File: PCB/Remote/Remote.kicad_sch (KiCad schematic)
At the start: 46 parts, among them J1 LCD, J2 DC, J3 TEMP, J4 LCD, J5 Reset, J6 USB-C-Socket-H, J7 TC2030-USB-NL-DS, U1 ESP32-S3-MINI-1, U2 SCD41, U3 MD8942, U4 TMP1075DSG, U5 GZP6816D, U8 VEML6040

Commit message: Moved PCB here
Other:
- title: 2" LCD -> Remote
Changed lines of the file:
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@@
 	(paper "A4")
 	(title_block
-		(title "2\" LCD")
+		(title "Remote")
 		(company "Adrian Kennard / Andrews & Arnold Ltd")
 		(comment 1 "@TheRealRevK")

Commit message: Case
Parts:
- D4: footprint RevK:SMD1010 -> RevK:SMD1010-Side
- U4: footprint Package_SON:WSON-8-1EP_2x2mm_P0.5mm_EP0.9x1.6mm_ThermalVias -> RevK:WSON-8-1EP_2x2mm_P0.5mm_EP0.9x1.6mm_ThermalVias-Side
- U8: footprint RevK:VEML6040 -> RevK:VEML6040-Side
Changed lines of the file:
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@@
 			)
 		)
-		(property "Footprint" "Package_SON:WSON-8-1EP_2x2mm_P0.5mm_EP0.9x1.6mm_ThermalVias"
+		(property "Footprint" "RevK:WSON-8-1EP_2x2mm_P0.5mm_EP0.9x1.6mm_ThermalVias-Side"
 			(at 252.73 116.84 0)
 			(effects
@@
 			)
 		)
-		(property "Footprint" "RevK:SMD1010"
+		(property "Footprint" "RevK:SMD1010-Side"
 			(at 162.56 43.815 0)
 			(effects
@@
 			)
 		)
-		(property "Footprint" "RevK:VEML6040"
+		(property "Footprint" "RevK:VEML6040-Side"
 			(at 254 126.365 0)
 			(effects

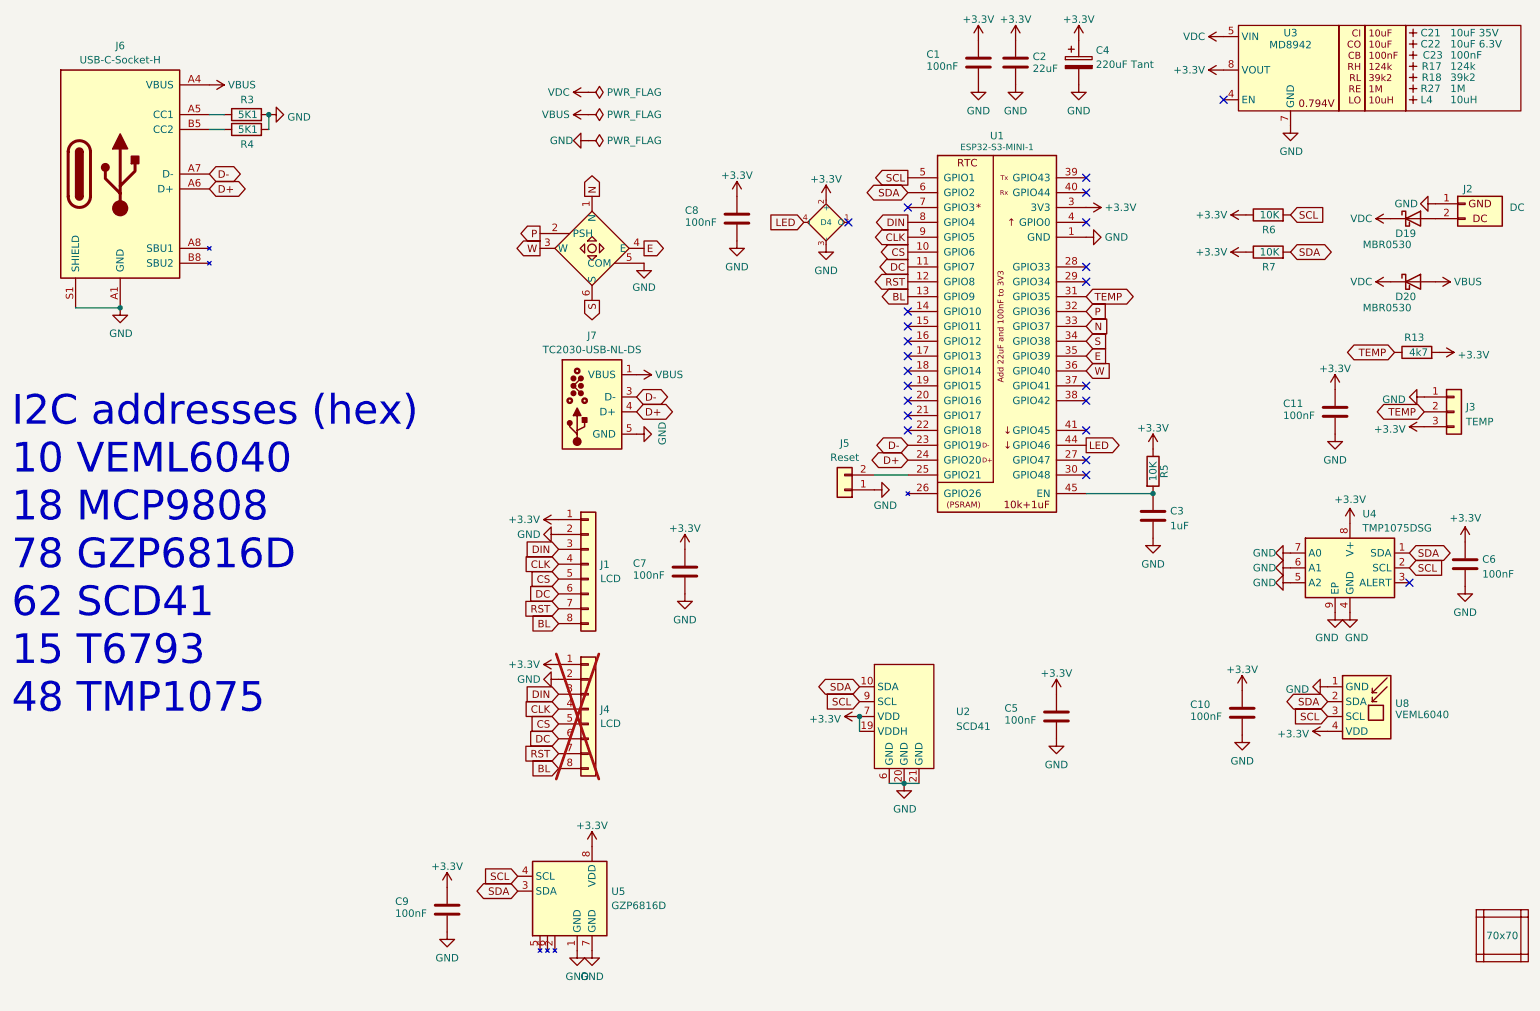
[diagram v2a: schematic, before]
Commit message: Change to SHT so humidity when no CO2
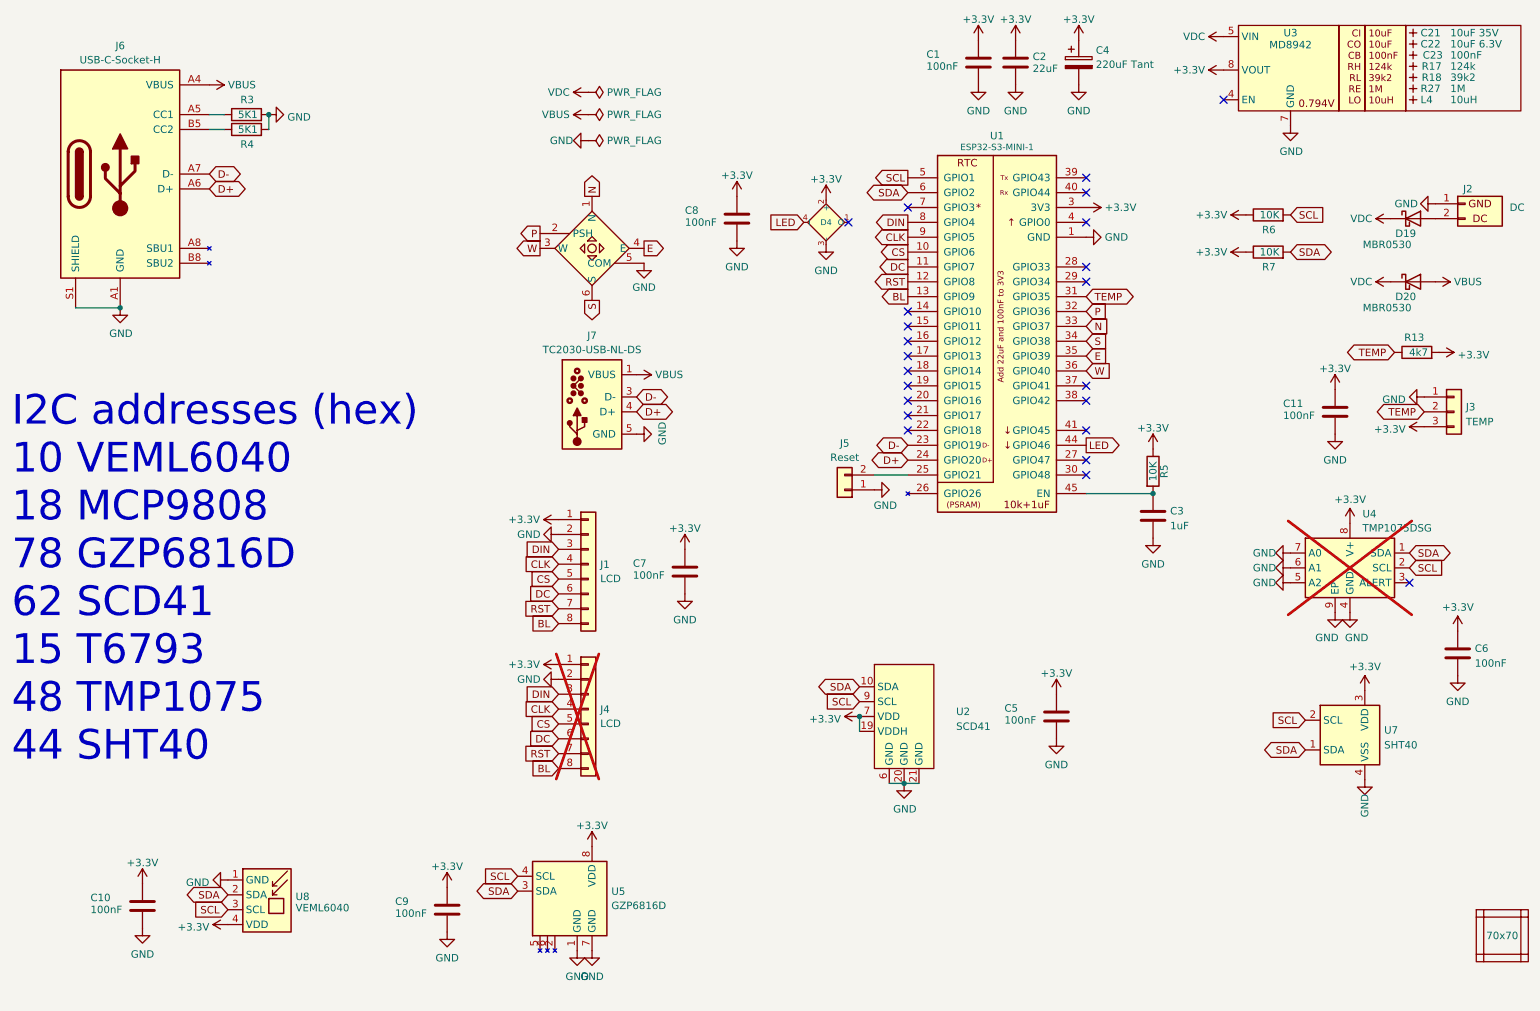
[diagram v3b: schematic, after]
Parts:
- added U7: SHT40, RevK:Sensirion_DFN-4_1.5x1.5mm_P0.5mm_SHT4x, symbol RevK:SHT40
- U4: now not fitted; now left out of the parts list
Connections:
- net +3.3V: now also U7.3 (VDD)
- net GND: now also U7.4 (VSS)
- net SCL: now also U7.2 (SCL)
- net SDA: now also U7.1 (SDA)
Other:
- note added: "I2C addresses (hex) 10 VEML6040 18 MCP9808 78 GZP6816D 62 SCD41 15 T6793 48 TMP1075 44 SHT40"
- note removed: "I2C addresses (hex) 10 VEML6040 18 MCP9808 78 GZP6816D 62 SCD41 15 T6793 48 TMP1075"
- moved on the sheet: C10, C6, U8

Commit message: Latest render
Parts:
- R13: MPN (none) -> C25900
- R17: MPN (none) -> C2933070
- R18: MPN (none) -> C7467415
- R27: MPN (none) -> C26083
- R3, R4: MPN (none) -> C25905
- R5, R6, R7: MPN (none) -> C25744
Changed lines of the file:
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@@
 			)
 		)
+		(property "MPN" "C25905"
+			(at 62.23 35.56 90)
+			(effects
+				(font
+					(size 1.27 1.27)
+				)
+				(hide yes)
+			)
+		)
 		(pin "1"
 		)
@@
 			)
 		)
+		(property "MPN" "C25905"
+			(at 62.23 33.02 90)
+			(effects
+				(font
+					(size 1.27 1.27)
+				)
+				(hide yes)
+			)
+		)
 		(pin "1"
 		)
@@
 			)
 		)
+		(property "MPN" "C25900"
+			(at 262.255 73.66 90)
+			(effects
+				(font
+					(size 1.27 1.27)
+				)
+				(hide yes)
+			)
+		)
 		(pin "1"
 		)
@@
 			)
 		)
+		(property "MPN" "C25744"
+			(at 236.855 50.165 90)
+			(effects
+				(font
+					(size 1.27 1.27)
+				)
+				(hide yes)
+			)
+		)
 		(pin "1"
 		)
@@
 			)
 		)
-		(property "Part No" ""
-			(at 261.62 28.575 0)
-			(effects
-				(font
-					(size 1.27 1.27)
-				)
-				(hide yes)
-			)
-		)
-		(property "Note" ""
+		(property "MPN" "C26083"
 			(at 261.62 28.575 0)
 			(effects
@@
 			)
 		)
-		(property "Part No" ""
-			(at 261.62 24.765 0)
-			(effects
-				(font
-					(size 1.27 1.27)
-				)
-				(hide yes)
-			)
-		)
-		(property "Note" ""
+		(property "MPN" "C2933070"
 			(at 261.62 24.765 0)
 			(effects
@@
 			)
 		)
+		(property "MPN" "C25744"
+			(at 217.17 93.98 90)
+			(effects
+				(font
+					(size 1.27 1.27)
+				)
+				(hide yes)
+			)
+		)
 		(pin "1"
 		)
@@
 			)
 		)
-		(property "Part No" ""
-			(at 261.62 26.67 0)
-			(effects
-				(font
-					(size 1.27 1.27)
-				)
-				(hide yes)
-			)
-		)
-		(property "Note" ""
-			(at 261.62 26.67 0)
+		(property "MPN" "C7467415"
+			(at 261.62 26.67 90)
 			(effects
 				(font
@@
 			(effects
 				(font
+					(size 1.27 1.27)
+				)
+				(hide yes)
+			)
+		)
+		(property "MPN" "C25744"
+			(at 236.855 56.515 90)
+			(effects
+				(font

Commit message: Tweaks
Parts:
- U5: footprint Package_LGA:Bosch_LGA-8_2x2.5mm_P0.65mm_ClockwisePinNumbering -> RevK:Bosch_LGA-8_2x2.5mm_P0.65mm_ClockwisePinNumbering
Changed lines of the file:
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@@
 			)
 		)
-		(property "Footprint" "Package_LGA:Bosch_LGA-8_2x2.5mm_P0.65mm_ClockwisePinNumbering"
+		(property "Footprint" "RevK:Bosch_LGA-8_2x2.5mm_P0.65mm_ClockwisePinNumbering"
 			(at 118.745 186.055 0)
 			(effects

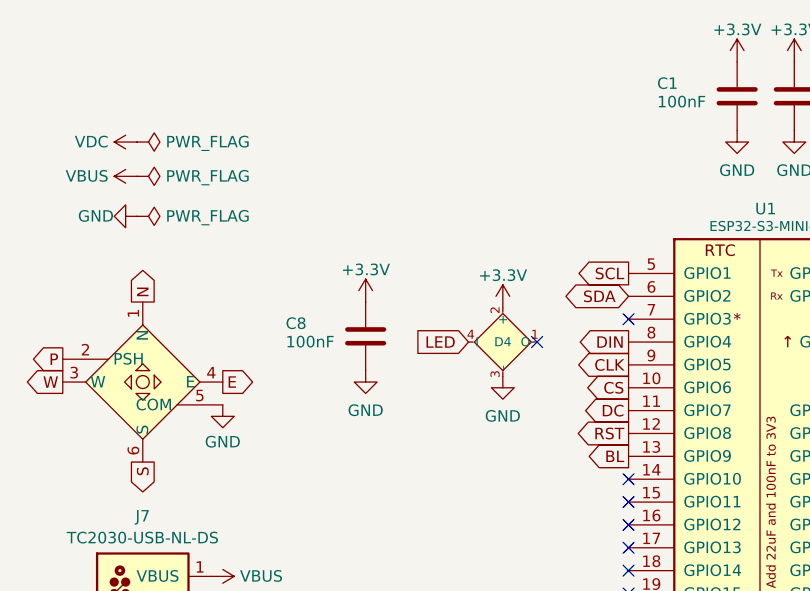
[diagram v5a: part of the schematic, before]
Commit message: More LEDs
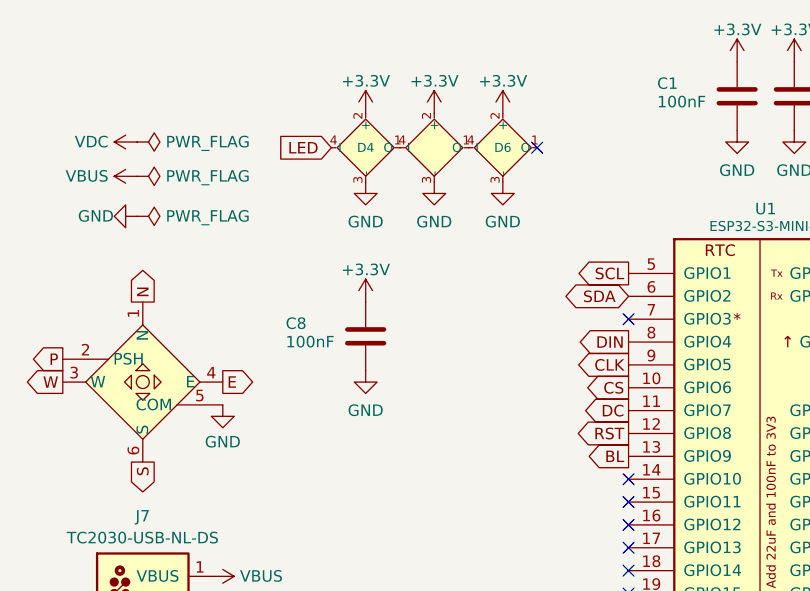
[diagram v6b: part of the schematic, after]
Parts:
- added D5, D6: XL-1010RGBC-WS2812B, RevK:SMD1010-Side, symbol RevK:WS2812B-1mm
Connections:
- net +3.3V: now also D5.2 (+), D6.2 (+)
- net GND: now also D5.3 (-), D6.3 (-)
- net at D4.1 (O): now also D5.4 (I)
- new net: D5.1 (O), D6.4 (I)
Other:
- moved on the sheet: D4

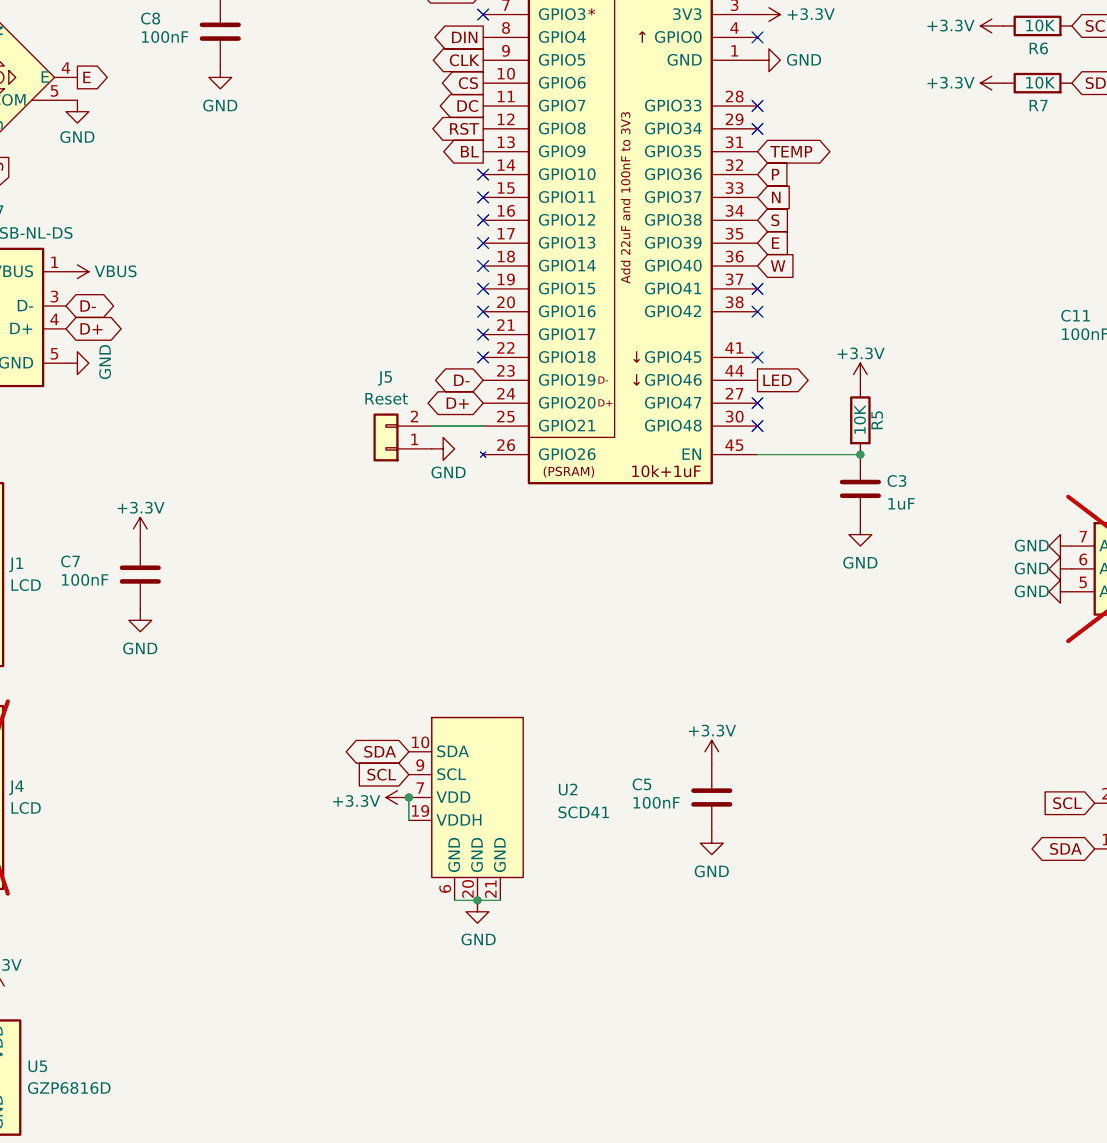
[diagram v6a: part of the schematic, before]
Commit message: Mic added
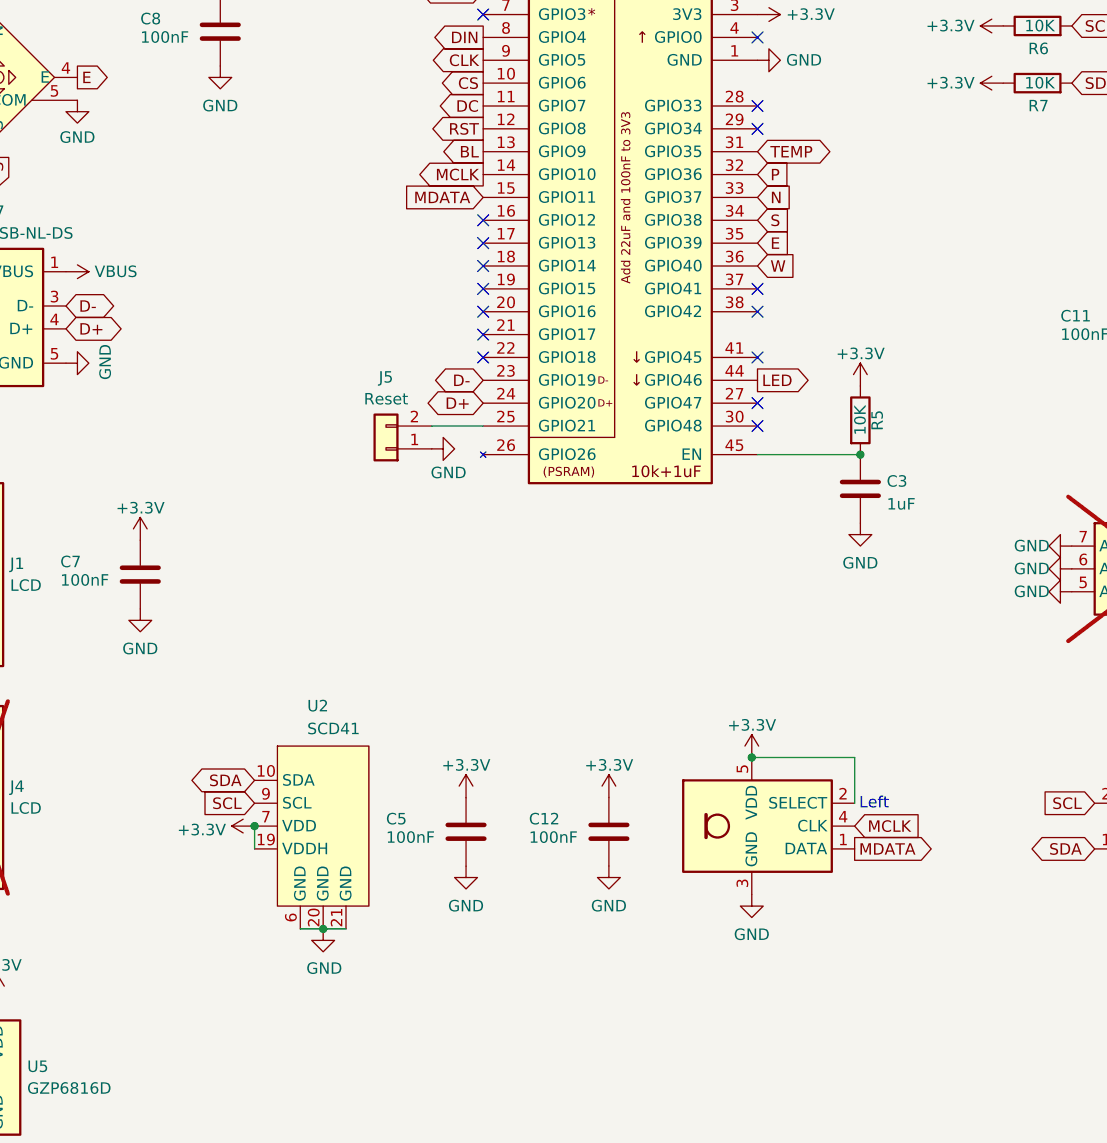
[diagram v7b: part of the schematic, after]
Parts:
- added C12: 100nF, RevK:C_0402, symbol Device:C
- added T1: T3902_MEMS_Mic, RevK:T3902_MEMS_Mic, symbol RevK:T3902_MEMS_Mic
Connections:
- net +3.3V: now also C12.1, T1.2 (SELECT), T1.5 (VDD)
- net GND: now also C12.2, T1.3 (GND)
- net MCLK: now reaches U1.14 (GPIO10)
- net MCLK: now also T1.4 (CLK)
- net MDATA: now reaches U1.15 (GPIO11)
- net MDATA: now also T1.1 (DATA)
- no-connect marks 23 -> 21
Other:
- note added: "Left"
- moved on the sheet: C5, U2
